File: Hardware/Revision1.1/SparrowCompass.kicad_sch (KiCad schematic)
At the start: 90 parts, among them IC1 NEO-M8N-0, IC2 LSM303AGRTR, IC3 DRV8834RGER, IC4 AEDR-8300-1Q2, IC6 MCP73833T-AMI_MF, J1 Conn_01x04, J2 Conn_Coaxial_Small, J3 USB4105-GF-A-060, J4 Conn_01x02, J5 Conn_01x02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

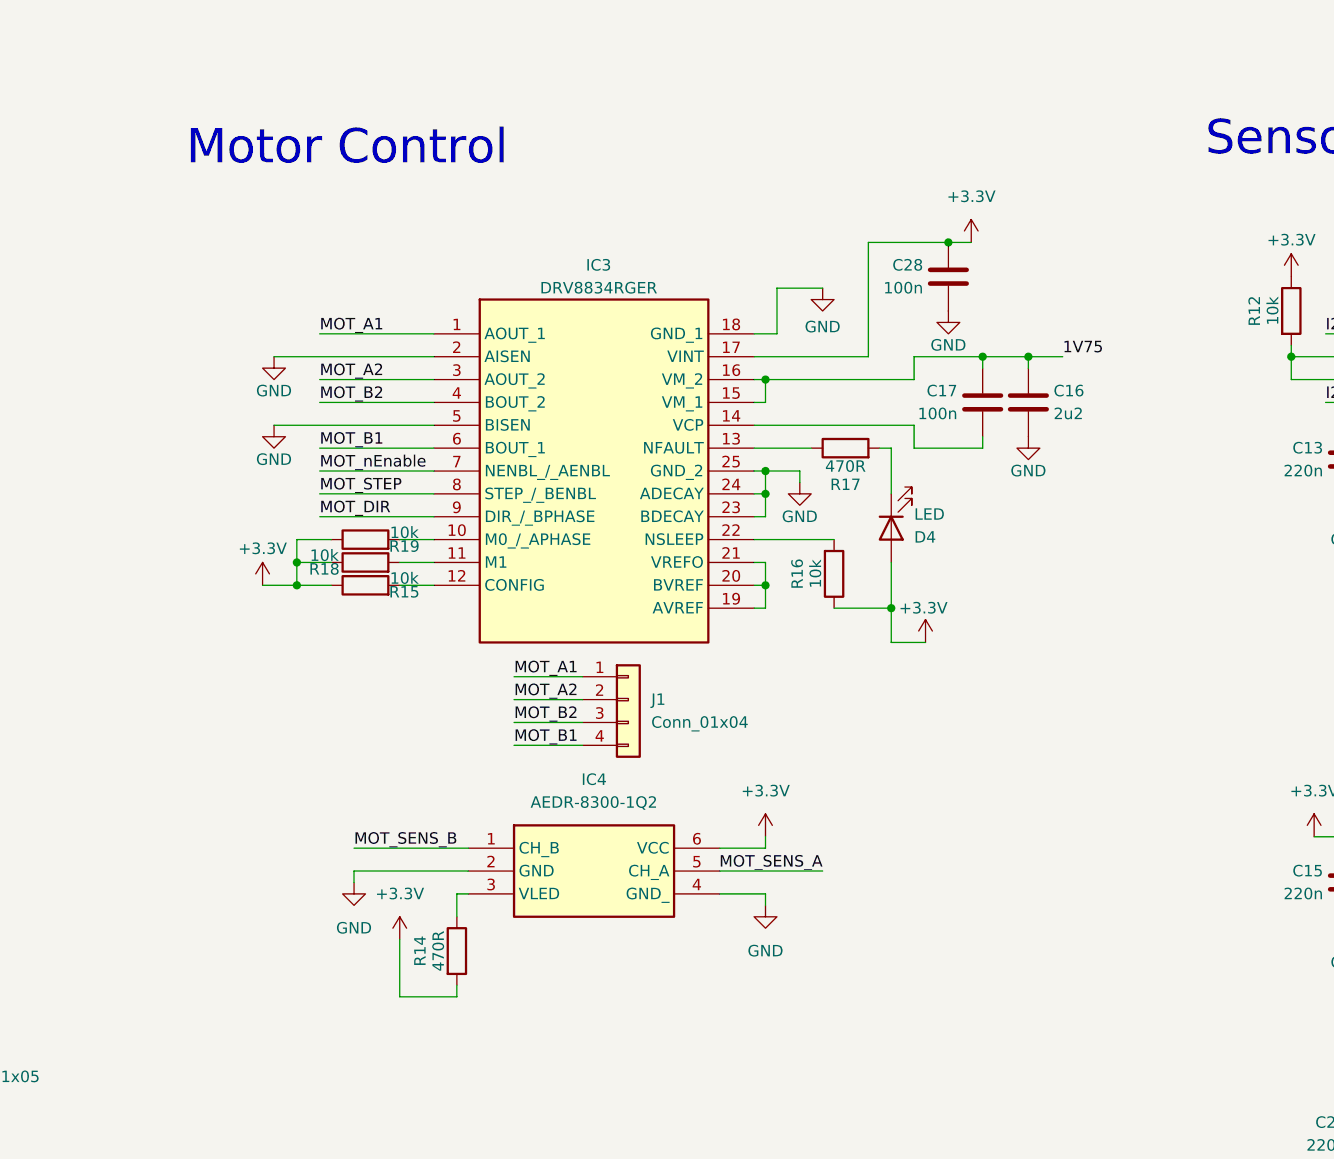
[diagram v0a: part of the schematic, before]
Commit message: init ardiono library
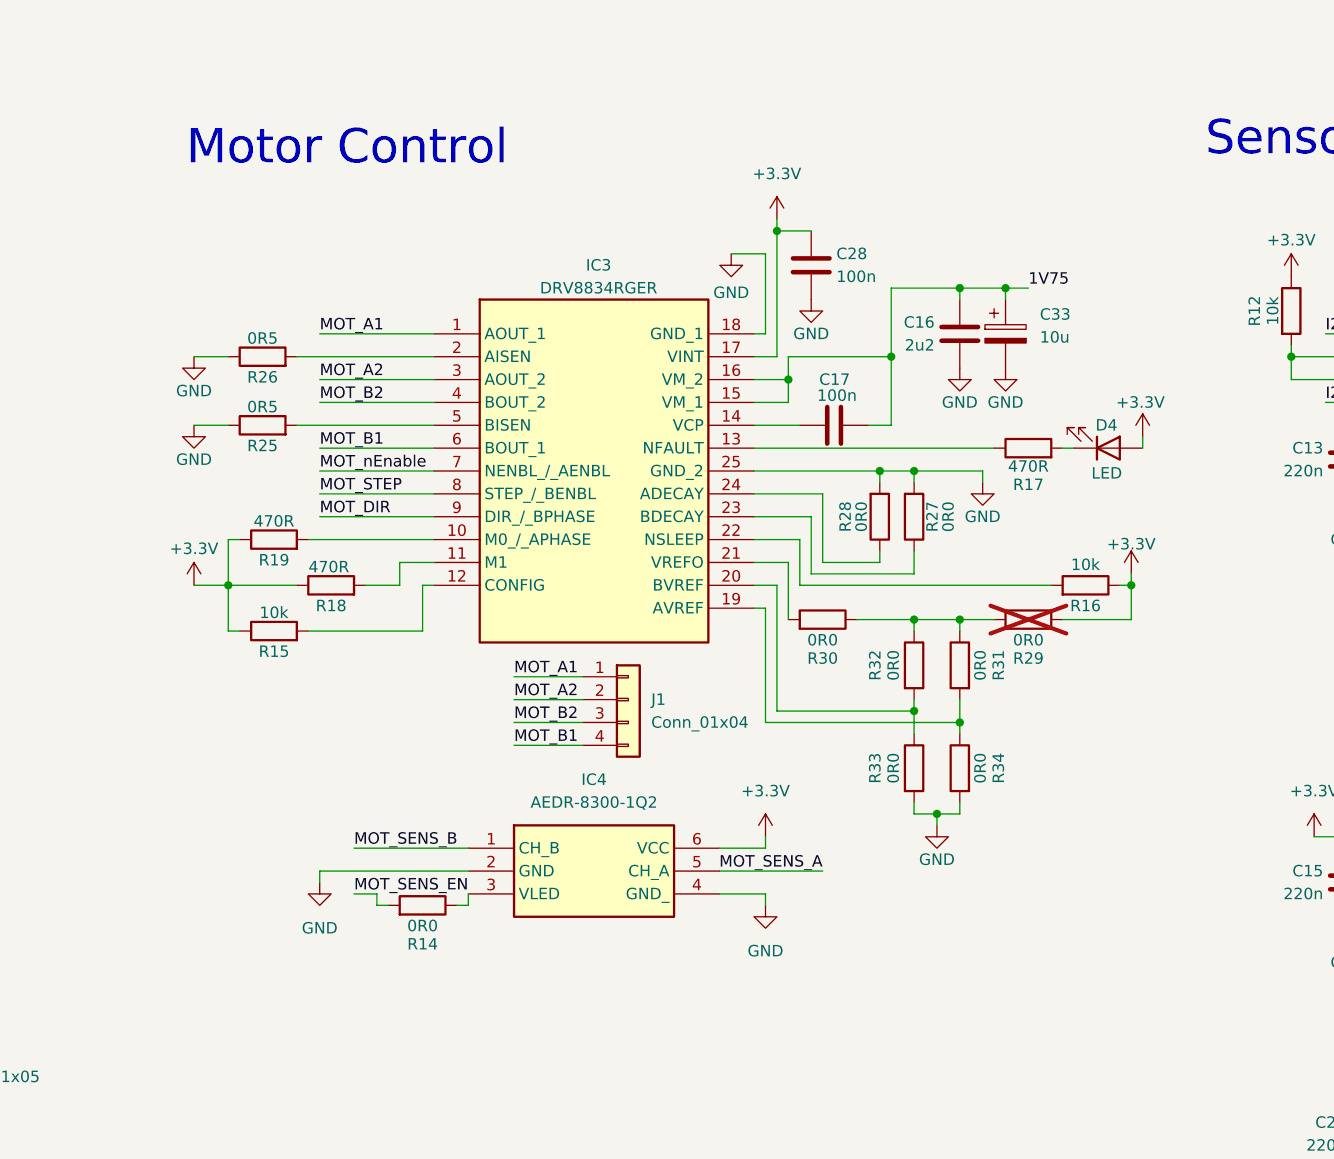
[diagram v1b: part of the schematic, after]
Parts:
- added C33: 10u, Capacitor_SMD:CP_Elec_4x5.3, symbol Device:C_Polarized
- added R25, R26: 0R5, Resistor_SMD:R_0603_1608Metric, symbol Device:R
- added R27, R28, R29, R30, R31, R32, R33, R34: 0R0, Resistor_SMD:R_0603_1608Metric, symbol Device:R
- R14: value 470R -> 0R0
- R18, R19: value 10k -> 470R
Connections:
- net +3.3V: now also R29.1; no longer R14.2
- net 1V75: now also C17.2, C33.1; no longer C17.1
- net GND: now also C33.2, R25.1, R26.1, R27.2, R28.2, R33.2, R34.2; no longer IC3.2 (AISEN), IC3.23 (BDECAY), IC3.24 (ADECAY), IC3.5 (BISEN)
- net at IC3.14 (VCP): now also C17.1; no longer C17.2
- new net: IC3.24 (ADECAY), R28.1
- new net: IC3.20 (BVREF), R32.2, R33.1
- new net: IC3.19 (AVREF), R31.2, R34.1
- new net: IC3.2 (AISEN), R26.2
- new net: IC3.21 (VREFO), R30.2
- new net: IC3.23 (BDECAY), R27.1
- new net: IC3.5 (BISEN), R25.2
- new net: R29.2, R30.1, R31.1, R32.1
- new net MOT_SENS_EN: R14.2
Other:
- moved on the sheet: C16, C17, C28, D4, R15, R16, R17, R18, R19
